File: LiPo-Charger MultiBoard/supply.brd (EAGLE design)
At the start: 50 x 50 mm, 22 parts, among them IC1 AP1084

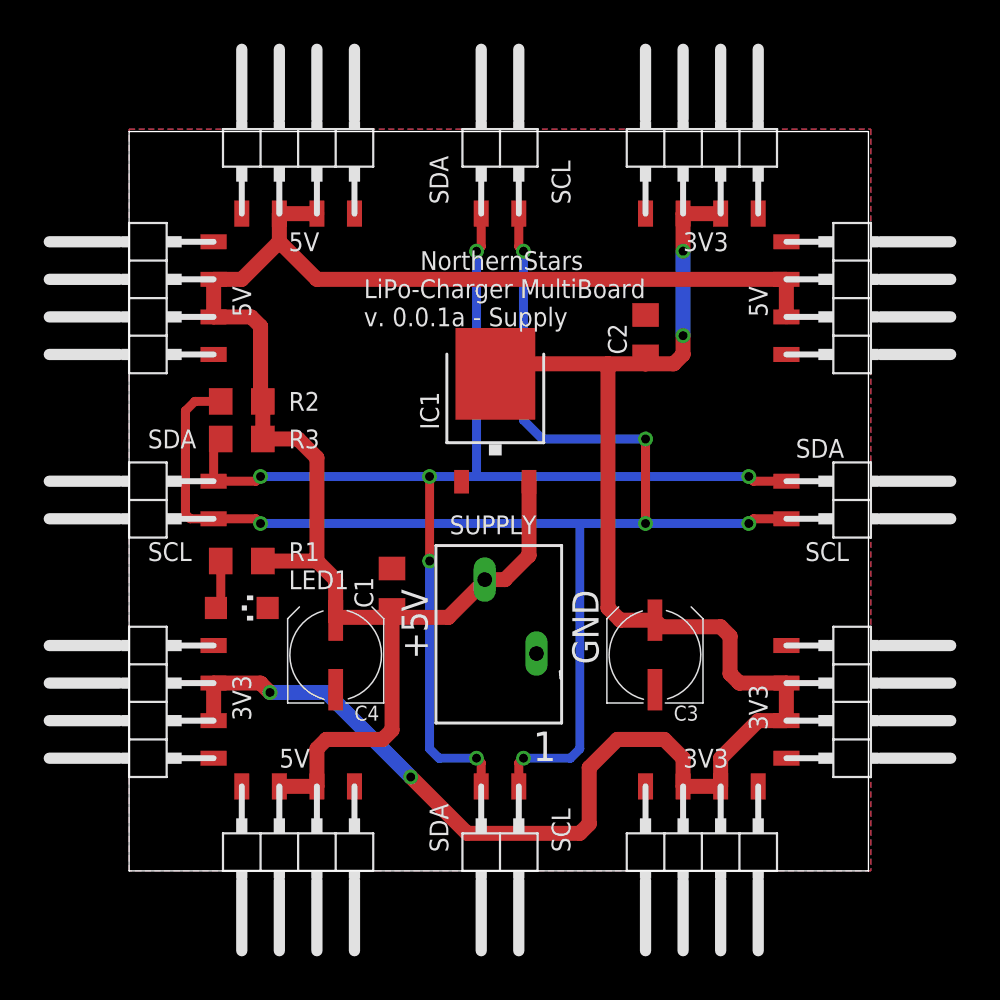
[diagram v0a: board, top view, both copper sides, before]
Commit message: Updated schematics and board. Added LibreOffice calculation for part lists.
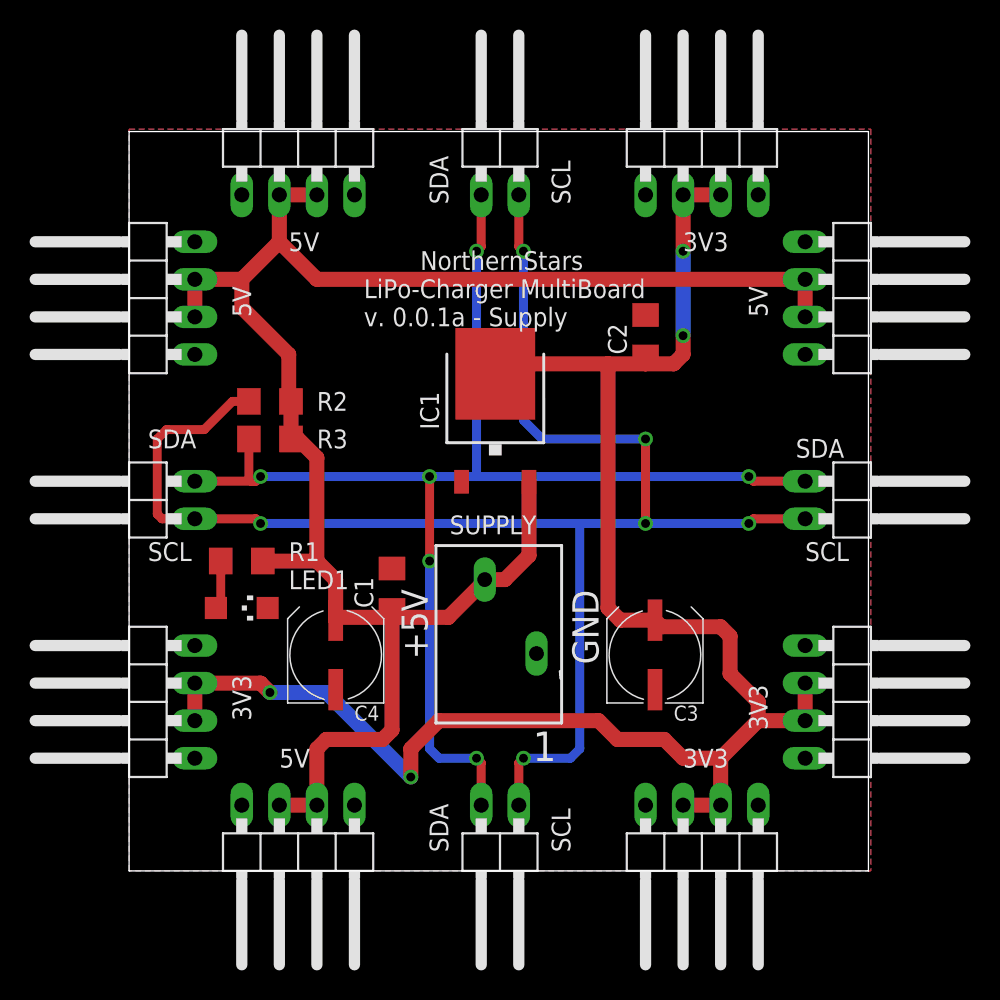
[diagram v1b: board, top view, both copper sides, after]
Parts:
- FEMALE_B, FEMALE_R, MALE_L, MALE_T: device pinhead-2:1X02SMD/90 -> pinhead-2:1X02/90
- FEMALE_BL, FEMALE_BR, FEMALE_RB, FEMALE_RT, MALE_LB, MALE_LT, MALE_TL, MALE_TR: device pinhead-2:1X04SMD/90 -> pinhead-2:1X04/90
- IC1: value AP1084 -> AP1084D33
- R1: value 130R -> 470R
- moved FEMALE_BL 2.54 mm to (11.4, 0.64)
- moved FEMALE_RB 2.54 mm to (49.5, 11.4)
- moved FEMALE_BR 2.54 mm to (38.7, 0.64)
- moved FEMALE_RT 2.54 mm to (49.5, 38.7)
- moved MALE_LB 2.54 mm to (0.64, 11.4)
- moved MALE_LT 2.54 mm to (0.64, 38.7)
- moved MALE_TL 2.54 mm to (11.4, 49.5)
- moved MALE_TR 2.54 mm to (38.7, 49.5)
- moved R2 1.91 mm to (9.53, 31.8)
- moved R3 1.91 mm to (9.53, 29.2)
- moved FEMALE_B 1.27 mm to (23.8, 0.64)
- moved FEMALE_R 1.27 mm to (49.5, 23.8)
- moved MALE_L 1.27 mm to (0.64, 26.4)
- moved MALE_T 1.27 mm to (26.4, 49.5)
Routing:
- net SCL: track 100.6 -> 109.3 mm
- net SDA: track 83.9 -> 88.8 mm
- net +5V: track 119.6 -> 123.8 mm
- net +3V3: track 116.3 -> 118.6 mm
